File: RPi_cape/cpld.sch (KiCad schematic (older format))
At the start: 67 parts, among them P15 Conn_02x05_Odd_Even, Q10 MMBT3904, Q9 MMBT3904, U29 LP5907MFX-3.3, U30 LP5907MFX-1.8, U31 DNP (5M40ZE64), U32 MIC1557, U33 5M80ZT100 / 5M240ZT100

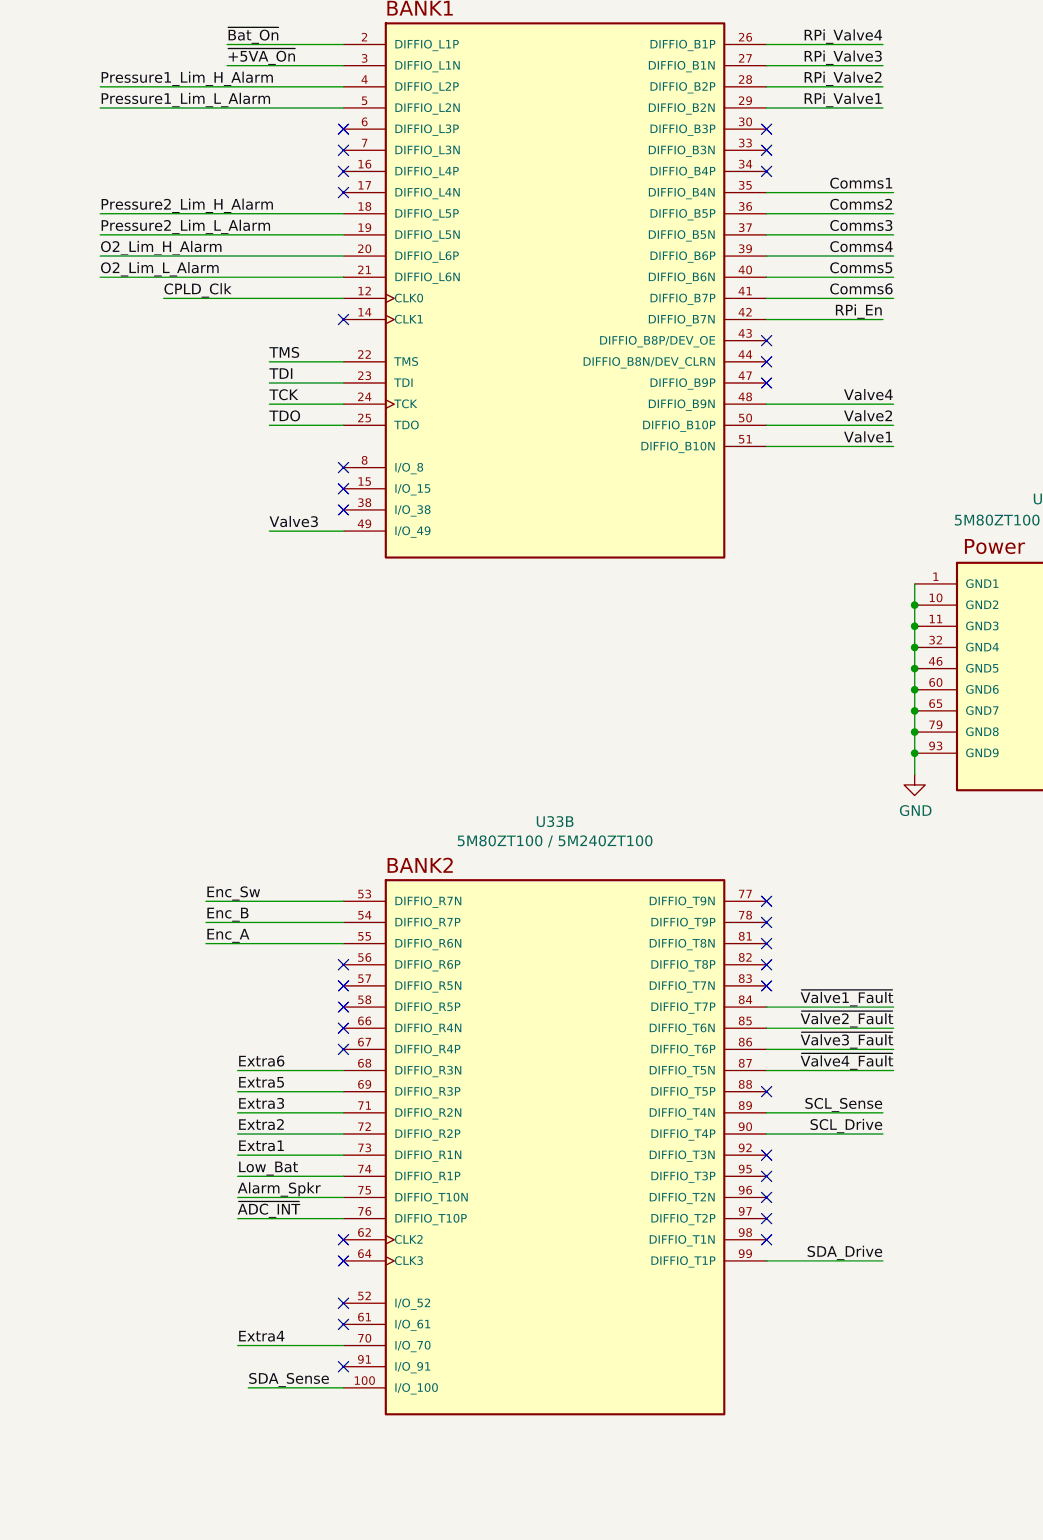
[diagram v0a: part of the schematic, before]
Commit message: Analog upgrades and extra encoder connectors
Renamed a few files
Removed "costing BOM" as difficult to keep up to date, easy to regenerate
Toughened under-voltage detect circuits by adding hysteresis to +5V detect for +BATT diode-OR (R236), filtering to power-down alarm detect input (C85)
Added connector options (J15, J21) for Grayhill C14-series rotary encoder with cable
Changed R190 from 3K to 2.4K to increase overhead on base current required for saturation, and consolidate BOM
Added 3 solderable testpoints for expanding CPLD pin options (TP44-46), adjusted some CPLD pin assignments to allow physical routing to pins
Fixed valve motion detector by changing comparator's hysteresis to AC-only, changing NPN's series resistor to 1K (allows low-enough DC level to count as logic low), and adding optional filtering cap C115 to offset divider
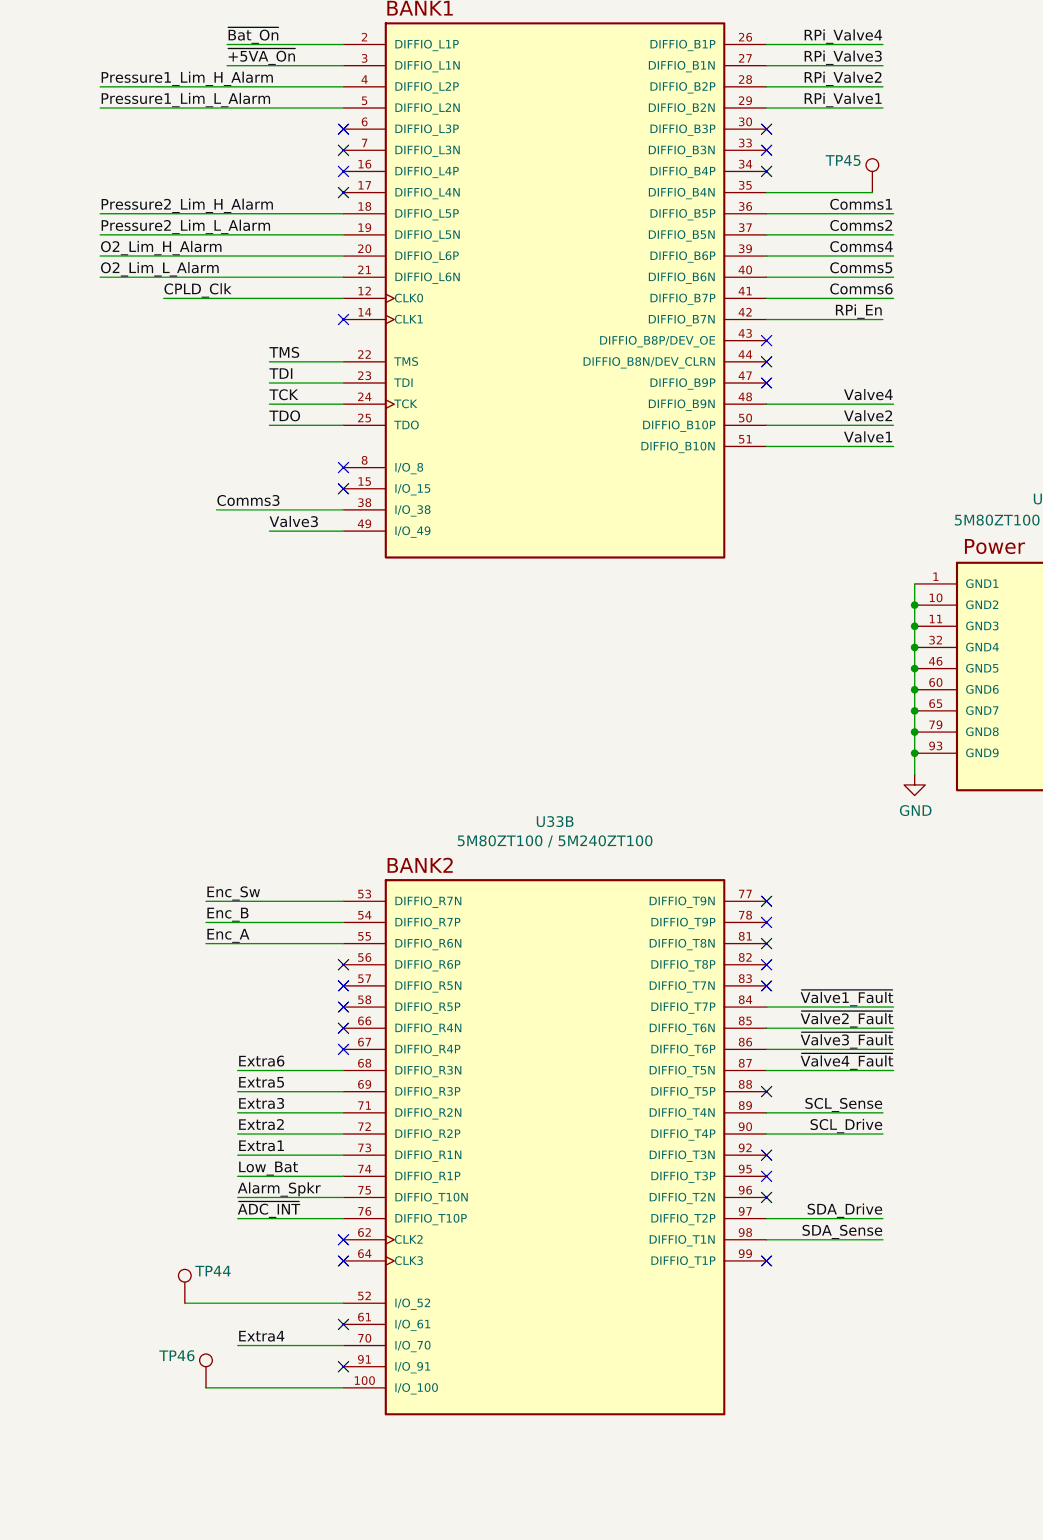
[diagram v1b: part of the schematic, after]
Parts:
- added TP44, TP45, TP46: TestPoint, TestPoint:TestPoint_Pad_1.0x1.0mm, symbol Connector:TestPoint
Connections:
- net Comms1: now also U33.36 (DIFFIO_B5P); no longer U33.35 (DIFFIO_B4N)
- net Comms2: now also U33.37 (DIFFIO_B5N); no longer U33.36 (DIFFIO_B5P)
- net Comms3: now also U33.38 (I/O_38); no longer U33.37 (DIFFIO_B5N)
- net SDA: now also U33.98 (DIFFIO_T1N); no longer U33.100 (I/O_100)
- net SDA_Drive: now also U33.97 (DIFFIO_T2P); no longer U33.99 (DIFFIO_T1P)
- net at U33.52 (I/O_52): now also TP44.1
- new net: TP45.1, U33.35 (DIFFIO_B4N)
- new net: TP46.1, U33.100 (I/O_100)
- no-connect marks 52 -> 49
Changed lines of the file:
@@
 encoding utf-8
 Sheet 15 15
-Title "CPLD"
+Title "Raspberry Pi Hat for JamVent Adaptation"
 Date ""
-Rev "1.7"
+Rev "1.8"
 Comp "US JamVent Team"
 Comment1 "Don Straney"
@@
 CPLD can be powered from backup battery when\nmain 5V power is out
 Wire Wire Line
-	12300 2300 12900 2300
-Text Label 12900 2300 2    50   ~ 0
-Comms1
-Wire Wire Line
 	12300 2400 12900 2400
 Text Label 12900 2400 2    50   ~ 0
-Comms2
+Comms1
 Wire Wire Line
 	12300 2500 12900 2500
 Text Label 12900 2500 2    50   ~ 0
+Comms2
+Wire Wire Line
+	10300 3800 9700 3800
+Text Label 9700 3800 0    50   ~ 0
 Comms3
 Wire Wire Line
@@
 Pressure1_Lim_H_Alarm
 Wire Wire Line
-	10300 7950 9850 7950
-Text Label 12850 7350 2    50   ~ 0
+	12300 7250 12850 7250
+Text Label 12850 7150 2    50   ~ 0
 SDA_Drive
-Text Label 9850 7950 0    50   ~ 0
+Text Label 12850 7250 2    50   ~ 0
 SDA_Sense
 Wire Wire Line
-	12850 7350 12300 7350
+	12850 7150 12300 7150
 Wire Wire Line
 	5450 8000 4750 8000
@@
 NoConn ~ 10300 7850
 NoConn ~ 10300 7650
-NoConn ~ 10300 7550
 NoConn ~ 10300 7350
 NoConn ~ 10300 7250
@@
 NoConn ~ 10300 3600
 NoConn ~ 10300 3700
-NoConn ~ 10300 3800
 NoConn ~ 12300 3000
 NoConn ~ 12300 3100
@@
 NoConn ~ 12300 6950
 NoConn ~ 12300 7050
-NoConn ~ 12300 7150
-NoConn ~ 12300 7250
 $Comp
 L Device:R R?
@@
 Wire Wire Line
 	9750 1700 10300 1700
+$Comp
+L Connector:TestPoint TP44
+U 1 1 5F052F66
+P 9550 7550
+F 0 "TP44" H 9600 7700 50  0000 L CNN
+F 1 "TestPoint" H 9608 7577 50  0001 L CNN
+F 2 "TestPoint:TestPoint_Pad_1.0x1.0mm" H 9750 7550 50  0001 C CNN
+F 3 "~" H 9750 7550 50  0001 C CNN
+	1    9550 7550
+	1    0    0    -1
+$EndComp
+Wire Wire Line
+	9550 7550 10300 7550
+$Comp
+L Connector:TestPoint TP46
+U 1 1 5F07D857
+P 9650 7950
+F 0 "TP46" H 9700 8100 50  0000 L CNN
+F 1 "TestPoint" H 9708 7977 50  0001 L CNN
+F 2 "TestPoint:TestPoint_Pad_1.0x1.0mm" H 9850 7950 50  0001 C CNN
+F 3 "~" H 9850 7950 50  0001 C CNN
+	1    9650 7950
+	-1   0    0    -1
+$EndComp
+Wire Wire Line
+	10300 7950 9650 7950
+$Comp
+L Connector:TestPoint TP45
+U 1 1 5F0937C5
+P 12800 2300
+F 0 "TP45" H 12850 2450 50  0000 L CNN
+F 1 "TestPoint" H 12858 2327 50  0001 L CNN
+F 2 "TestPoint:TestPoint_Pad_1.0x1.0mm" H 13000 2300 50  0001 C CNN
+F 3 "~" H 13000 2300 50  0001 C CNN
+	1    12800 2300
+	-1   0    0    -1
+$EndComp
+Wire Wire Line
+	12800 2300 12300 2300
+NoConn ~ 12300 7350
 $EndSCHEMATC

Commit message: Admin (naming, license), improvements based on testing
Updated name on schematic, PCB silkscreen
Added 3 mounting holes on inside area of board for better mechanical robustness
Removed extra unused pressure sensor barb packages from library
Fixed Phoenix spring connector footprints, and added 3D models from Phoenix website
Added 3D models to TE encoder connector footprints, QFP-100 for CPLD, and 5019 testpoint
Changed DIAG_EN pin connection from valve drivers from +24V (too high) to +3.3V
Added CERN licensing terms
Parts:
- TP21, TP22, TP23, TP24, TP25, TP26, TP27, TP28, TP42, TP43: footprint TestPoint:TestPoint_Keystone_5019_Minature -> Ventilator:TestPoint_Keystone_5019_Minature
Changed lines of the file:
@@
 encoding utf-8
 Sheet 15 15
-Title "Raspberry Pi Hat for JamVent Adaptation"
+Title "GlobalVent Stand-Alone Controller"
 Date ""
-Rev "1.9"
-Comp "US JamVent Team"
-Comment1 "Don Straney"
-Comment2 ""
+Rev "1.10"
+Comp "US GlobalVent Team"
+Comment1 "Licensed under CERN-OHL-S v2"
+Comment2 "Don Straney"
 Comment3 ""
 Comment4 ""
@@
 F 0 "TP27" H 2900 8750 50  0000 R CNN
 F 1 "TestPoint_Flag" H 2856 8653 50  0001 R CNN
-F 2 "TestPoint:TestPoint_Keystone_5019_Minature" H 3100 8650 50  0001 C CNN
+F 2 "Ventilator:TestPoint_Keystone_5019_Minature" H 3100 8650 50  0001 C CNN
 F 3 "~" H 3100 8650 50  0001 C CNN
 F 4 "Keystone" H 2900 8650 50  0001 C CNN "Manufacturer"
@@
 F 0 "TP28" H 2900 9800 50  0000 R CNN
 F 1 "TestPoint_Flag" H 2856 9703 50  0001 R CNN
-F 2 "TestPoint:TestPoint_Keystone_5019_Minature" H 3100 9700 50  0001 C CNN
+F 2 "Ventilator:TestPoint_Keystone_5019_Minature" H 3100 9700 50  0001 C CNN
 F 3 "~" H 3100 9700 50  0001 C CNN
 F 4 "Keystone" H 2900 9700 50  0001 C CNN "Manufacturer"
@@
 F 0 "TP22" H 2850 2950 50  0000 R CNN
 F 1 "TestPoint_Flag" H 2806 2853 50  0001 R CNN
-F 2 "TestPoint:TestPoint_Keystone_5019_Minature" H 3050 2850 50  0001 C CNN
+F 2 "Ventilator:TestPoint_Keystone_5019_Minature" H 3050 2850 50  0001 C CNN
 F 3 "~" H 3050 2850 50  0001 C CNN
 F 4 "Keystone" H 2850 2850 50  0001 C CNN "Manufacturer"
@@
 F 0 "TP23" H 2850 3150 50  0000 R CNN
 F 1 "TestPoint_Flag" H 2806 3053 50  0001 R CNN
-F 2 "TestPoint:TestPoint_Keystone_5019_Minature" H 3050 3050 50  0001 C CNN
+F 2 "Ventilator:TestPoint_Keystone_5019_Minature" H 3050 3050 50  0001 C CNN
 F 3 "~" H 3050 3050 50  0001 C CNN
 F 4 "Keystone" H 2850 3050 50  0001 C CNN "Manufacturer"
@@
 F 0 "TP24" H 2850 3350 50  0000 R CNN
 F 1 "TestPoint_Flag" H 2806 3253 50  0001 R CNN
-F 2 "TestPoint:TestPoint_Keystone_5019_Minature" H 3050 3250 50  0001 C CNN
+F 2 "Ventilator:TestPoint_Keystone_5019_Minature" H 3050 3250 50  0001 C CNN
 F 3 "~" H 3050 3250 50  0001 C CNN
 F 4 "Keystone" H 2850 3250 50  0001 C CNN "Manufacturer"
@@
 F 0 "TP25" H 2850 3550 50  0000 R CNN
 F 1 "TestPoint_Flag" H 2806 3453 50  0001 R CNN
-F 2 "TestPoint:TestPoint_Keystone_5019_Minature" H 3050 3450 50  0001 C CNN
+F 2 "Ventilator:TestPoint_Keystone_5019_Minature" H 3050 3450 50  0001 C CNN
 F 3 "~" H 3050 3450 50  0001 C CNN
 F 4 "Keystone" H 2850 3450 50  0001 C CNN "Manufacturer"
@@
 F 0 "TP26" H 2850 3750 50  0000 R CNN
 F 1 "TestPoint_Flag" H 2806 3653 50  0001 R CNN
-F 2 "TestPoint:TestPoint_Keystone_5019_Minature" H 3050 3650 50  0001 C CNN
+F 2 "Ventilator:TestPoint_Keystone_5019_Minature" H 3050 3650 50  0001 C CNN
 F 3 "~" H 3050 3650 50  0001 C CNN
 F 4 "Keystone" H 2850 3650 50  0001 C CNN "Manufacturer"
@@
 F 0 "TP21" H 2850 2750 50  0000 R CNN
 F 1 "TestPoint_Flag" H 2806 2653 50  0001 R CNN
-F 2 "TestPoint:TestPoint_Keystone_5019_Minature" H 3050 2650 50  0001 C CNN
+F 2 "Ventilator:TestPoint_Keystone_5019_Minature" H 3050 2650 50  0001 C CNN
 F 3 "~" H 3050 2650 50  0001 C CNN
 F 4 "Keystone" H 2850 2650 50  0001 C CNN "Manufacturer"
@@
 F 0 "TP42" H 1050 8500 50  0000 R CNN
 F 1 "TestPoint_Flag" H 756 8353 50  0001 R CNN
-F 2 "TestPoint:TestPoint_Keystone_5019_Minature" H 1000 8350 50  0001 C CNN
+F 2 "Ventilator:TestPoint_Keystone_5019_Minature" H 1000 8350 50  0001 C CNN
 F 3 "~" H 1000 8350 50  0001 C CNN
 F 4 "Keystone" H 800 8350 50  0001 C CNN "Manufacturer"
@@
 F 0 "TP43" H 1050 8800 50  0000 R CNN
 F 1 "TestPoint_Flag" H 756 8653 50  0001 R CNN
-F 2 "TestPoint:TestPoint_Keystone_5019_Minature" H 1000 8650 50  0001 C CNN
+F 2 "Ventilator:TestPoint_Keystone_5019_Minature" H 1000 8650 50  0001 C CNN
 F 3 "~" H 1000 8650 50  0001 C CNN
 F 4 "Keystone" H 800 8650 50  0001 C CNN "Manufacturer"

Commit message: Design update based on changed software/firmware/pneumatics reqs
Swapped Max V CPLD for Max 10 FPGA
Removed +1.8V regulator and monitoring (in power-down alarm) because Max 10 FPGA has internal regulator
Changed FPGA's valve-enable pull-downs from 1K to 10K because Max 10 floats the outputs during power-up/programming (instead of Max V's internal pull-ups)
Changed low-pressure sensor from BMP388 to MS5607 for more manufacturable footprint / high availability, and moved all digital pressure sensors to daughterboard for repairability
Changed single op-amps in analog pressure sensor inputs / valve motion detect circuits to TLV6001 for better bias current, correct footprint
Removed excessive DNP components in analog pressure sensor inputs to ease routing with new op-amps
Added double-inverted hysteresis circuit to valve motion detect that won't drive U38's '+' input above the rail and cause latchup
Added optional pull-down resistors to valve-motiion-detect op-amps to allow output voltages to swing to zero
Added optional filter caps to ADC sensor inputs
Added pull-down to O2 sensor input for testing with sensor unplugged
Increased ADC input resistors (in analog sensor inputs) from 1K to 3.3K to avoid "lifting" +3.3V rail voltage in case of fault
Increased hole sizes to 3.7 mm for fitting #6 screws, to match some threaded vibration-damping bumpers from Joost
Fixed F.Fab-layer component reference text in custom footprints
Updated manufacturing files
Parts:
- removed D46: Orange, Ventilator:LED_0805_2012Metric, symbol Device:LED
- removed Q10, Q9: MMBT3904, Ventilator:SOT-23, symbol Transistor_BJT:MMBT3904
- removed TP28: TestPoint_Flag, Ventilator:TestPoint_Keystone_5019_Minature, symbol Connector:TestPoint_Flag
- removed U30: LP5907MFX-1.8, Ventilator:SOT-23-5, symbol Regulator_Linear:LP5907MFX-1.8
- removed U31: DNP (5M40ZE64), Ventilator:QFP40P900X900X120-65N, symbol Ventilator:5M40ZE64C5N
- removed U33: 5M80ZT100 / 5M240ZT100, Ventilator:QFP50P1600X1600X120-100N, symbol Ventilator:5M80ZT100C5N
- added C116, C117, C118, C119, C120, C121, C123, C124, C125, C126, C127, C128, C129, C130, C131, C132, C133: 100nF 50V X7R, Capacitor_SMD:C_0603_1608Metric, symbol Device:C
- added C122, C136, C137: 10pF 50V NP0, Capacitor_SMD:C_0603_1608Metric, symbol Device:C
- added C134, C135: 1uF 16V X7R, Capacitor_SMD:C_0805_2012Metric, symbol Device:C
- added D14, D2: BAT54C, Package_TO_SOT_SMD:SOT-23, symbol Device:D_Schottky_x2_KCom_AAK
- added FB1: TBD, Inductor_SMD:L_0805_2012Metric, symbol Device:Ferrite_Bead
- added R131, R132, R237, R238, R239: 10K, Resistor_SMD:R_1206_3216Metric, symbol Device:R
- added R221: 0, Resistor_SMD:R_1206_3216Metric, symbol Device:R
- added U30: 10M08SAE144C8G, Ventilator:LQFP50P2200X2200X160-145N, symbol Ventilator:10M08SAE144C8G
- C71, C73: value 1uF 16V X7R -> 100nF 50V X7R; footprint Capacitor_SMD:C_0805_2012Metric -> Capacitor_SMD:C_0603_1608Metric; Manufacturer Kemet -> AVX; Part Number C0805C105K4RACTU -> 06035C104JAT2A
- C74, P15, R186: DNI (none) -> DNI
- C75: value DNP -> 100nF 50V X7R; footprint Capacitor_SMD:C_1210_3225Metric -> Capacitor_SMD:C_0603_1608Metric; Manufacturer (none) -> AVX; Part Number (none) -> 06035C104JAT2A
- C86: value 1uF 16V X7R -> 10pF 50V NP0; footprint Capacitor_SMD:C_0805_2012Metric -> Capacitor_SMD:C_0603_1608Metric; Manufacturer Kemet -> (none); Part Number C0805C105K4RACTU -> (none)
- R152: value 10K -> 1K; Part Number RK73H2BTTD1002F -> RK73H2BTTD1001F
- R153: value 10K -> 0; Manufacturer KOA Speer -> Panasonic; Part Number RK73H2BTTD1002F -> ERJ-8GEY0R00V
- R154: value 10K -> DNP; DNI (none) -> DNI; Manufacturer KOA Speer -> (none); Part Number RK73H2BTTD1002F -> (none)
- R159: value 100 -> 10K; Part Number RK73H2BTTD1000F -> RK73H2BTTD1002F
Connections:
- net SCL_Drive is gone; now on an unnamed net: R154.2
- net SDA_Drive is gone; now on net +3V3: R153.2
- net +3V3: now also C71.2, C73.2, C75.2, C87.2, C90.2, R159.1, C116.2, C117.2, C118.2, C120.2, C121.2, C123.2, C124.2, C126.2, C127.2, C129.2, C131.2, C133.2, C135.2, D14.3 (K), D2.3 (K), FB1.1, R131.1, R132.1, R221.2, R237.1, R238.1, R239.1, U30.1 (VCC_ONE1), U30.103 (VCCIO6_2), U30.108 (VCC_ONE7), U30.109 (VCC_ONE8), U30.115 (VCC_ONE9), U30.117 (VCCIO7), U30.128 (VCCIO8_1), U30.139 (VCCIO8_2), U30.144 (VCC_ONE10), U30.23 (VCCIO1B), U30.31 (VCCIO2), U30.36 (VCC_ONE2), U30.37 (VCC_ONE3), U30.40 (VCCIO3_1), U30.49 (VCCIO3_2), U30.5 (ADC_VREF), U30.51 (VCC_ONE4), U30.67 (VCCIO4), U30.72 (VCC_ONE5), U30.73 (VCC_ONE6), U30.82 (VCCIO5), U30.9 (VCCIO1A), U30.94 (VCCIO6_1)
- net Alarm_Spkr: now also U30.111 (IO,(DIFFIO_RX_T1N,DIFFOUT_T1N))
- net CPLD_Clk: now also U30.27 (IO,CLK0P,(DIFFIO_RX_L18P,DIFFOUT_L18P))
- net Comms1: now also U30.56 (IO,(DIFFIO_TX_RX_B12P,DIFFOUT_B12P))
- net Comms2: now also U30.57 (IO,(DIFFIO_TX_RX_B14N,DIFFOUT_B14N))
- net Comms3: now also U30.58 (IO,(DIFFIO_TX_RX_B14P,DIFFOUT_B14P))
- net Comms4: now also U30.59 (IO,(DIFFIO_TX_RX_B16N,DIFFOUT_B16N))
- net Comms5: now also U30.60 (IO,(DIFFIO_TX_RX_B16P,DIFFOUT_B16P))
- net Comms6: now also U30.61 (IO,VREFB4N0)
- net Enc_A: now also U30.87 (IO,(DIFFIO_RX_R10N,DIFFOUT_R10N))
- net Enc_B: now also U30.86 (IO,(DIFFIO_RX_R11N,DIFFOUT_R11N))
- net Enc_Sw: now also U30.79 (IO,(DIFFIO_RX_R7P,DIFFOUT_R7P))
- net Extra1: now also U30.100 (IO,(DIFFIO_RX_R28P,DIFFOUT_R28P))
- net Extra2: now also U30.99 (IO,(DIFFIO_RX_R27P,DIFFOUT_R27P))
- net Extra3: now also U30.98 (IO,DPCLK2,(DIFFIO_RX_R26N,DIFFOUT_R26N))
- net Extra4: now also U30.90 (IO,CLK3P,(DIFFIO_RX_R16P,DIFFOUT_R16P))
- net Extra5: now also U30.89 (IO,CLK2N,(DIFFIO_RX_R14N,DIFFOUT_R14N))
- net Extra6: now also U30.88 (IO,CLK2P,(DIFFIO_RX_R14P,DIFFOUT_R14P))
- net GND: now also C75.1, R154.1, C116.1, C117.1, C118.1, C119.1, C120.1, C121.1, C122.1, C123.1, C124.1, C125.1, C126.1, C127.1, C128.1, C129.1, C130.1, C131.1, C132.1, C133.1, C134.1, C135.1, C136.1, C137.1, U30.104 (GND7), U30.116 (GND8), U30.122 (IO,DEV_OE), U30.125 (GND9), U30.133 (GND10), U30.137 (GND11), U30.142 (GND12), U30.145 (EXP), U30.3 (ANAIN1), U30.4 (REFGND), U30.42 (GND1), U30.53 (GND2), U30.63 (GND3), U30.68 (GND4), U30.83 (GND5), U30.95 (GND6); no longer C75.2
- net Low_Bat: now also U30.102 (IO,(DIFFIO_RX_R28N,DIFFOUT_R28N))
- net O2_Lim_H_Alarm: now also U30.11 (IO,ADC1IN5,(DIFFIO_RX_L5N,DIFFOUT_L5N))
- net O2_Lim_L_Alarm: now also U30.12 (IO,ADC1IN6,(DIFFIO_RX_L5P,DIFFOUT_L5P))
- net Pressure1_Lim_H_Alarm: now also U30.6 (IO,ADC1IN1,(DIFFIO_RX_L1N,DIFFOUT_L1N))
- net Pressure1_Lim_L_Alarm: now also U30.7 (IO,ADC1IN2,(DIFFIO_RX_L1P,DIFFOUT_L1P))
- net Pressure2_Lim_H_Alarm: now also U30.8 (IO,ADC1IN3,(DIFFIO_RX_L3N,DIFFOUT_L3N))
- net Pressure2_Lim_L_Alarm: now also U30.10 (IO,ADC1IN4,(DIFFIO_RX_L3P,DIFFOUT_L3P))
- net RPi_En: now also U30.62 (IO4_1)
- net RPi_Valve1: now also U30.47 (IO,(DIFFIO_TX_RX_B7P,DIFFOUT_B7P))
- net RPi_Valve2: now also U30.46 (IO,(DIFFIO_TX_RX_B7N,DIFFOUT_B7N))
- net RPi_Valve3: now also U30.45 (IO,(DIFFIO_TX_RX_B5P,DIFFOUT_B5P))
- net RPi_Valve4: now also U30.44 (IO,(DIFFIO_TX_RX_B5N,DIFFOUT_B5N))
- net SCL: now also U30.131 (IO,(DIFFIO_RX_T20N,DIFFOUT_T20N))
- net SDA: now also U30.132 (IO,(DIFFIO_RX_T22P,DIFFOUT_T22P))
- net TCK: now also C136.2, D2.2 (A), U30.18 (IO,TCK,(DIFFIO_RX_L11P,DIFFOUT_L11P))
- net TDI: now also C86.2, D14.2 (A), R238.2, U30.19 (IO,TDI,(DIFFIO_RX_L12N,DIFFOUT_L12N))
- net TDO: now also C137.2, D14.1 (A), U30.20 (IO,TDO,(DIFFIO_RX_L12P,DIFFOUT_L12P))
- net TMS: now also C122.2, D2.1 (A), R239.2, U30.16 (IO,TMS,(DIFFIO_RX_L11N,DIFFOUT_L11N))
- net Valve1: now also U30.78 (IO5_1)
- net Valve2: now also U30.77 (IO,(DIFFIO_RX_R1N,DIFFOUT_R1N))
- net Valve3: now also U30.76 (IO,(DIFFIO_RX_R2N,DIFFOUT_R2N))
- net Valve4: now also U30.75 (IO,(DIFFIO_RX_R1P,DIFFOUT_R1P))
- net ~+5VA_On: now also U30.101 (IO,(DIFFIO_RX_R27N,DIFFOUT_R27N))
- net ~ADC_INT: now also U30.130 (IO,(DIFFIO_RX_T20P,DIFFOUT_T20P))
- net ~Bat_On: now also U30.106 (IO,(DIFFIO_RX_R33N,DIFFOUT_R33N))
- net ~Valve1_Fault: now also U30.119 (IO,(DIFFIO_RX_T10N,DIFFOUT_T10N))
- net ~Valve2_Fault: now also U30.120 (IO,(DIFFIO_RX_T16P,DIFFOUT_T16P))
- net ~Valve3_Fault: now also U30.123 (IO,VREFB8N0)
- net ~Valve4_Fault: now also U30.124 (IO,(DIFFIO_RX_T19P,DIFFOUT_T19P))
- net at TP45.1: now also U30.91 (IO,CLK3N,(DIFFIO_RX_R16N,DIFFOUT_R16N))
- net at TP46.1: now also U30.135 (IO8_1)
- net at TP44.1: now also U30.14 (IO,ADC1IN8,(DIFFIO_RX_L7P,DIFFOUT_L7P))
- net at C70.2, R185.1, R186.1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: no longer C71.2
- net at R153.1: now also U30.126 (IO,CONFIG_SEL)
- removed net +1V8: C73.2, C75.1, C86.2, C87.2, C90.2, R159.2
- new net: R221.1, U30.121 (IO,DEV_CLRN,(DIFFIO_RX_T16N,DIFFOUT_T16N))
- new net: R237.2, U30.129 (NCONFIG)
- new net: R159.2, U30.134 (IO,CRC_ERROR,(DIFFIO_RX_T22N,DIFFOUT_T22N))
- new net: R131.2, U30.138 (IO,CONF_DONE,(DIFFIO_RX_T24N,DIFFOUT_T24N))
- new net +3.3VA: C119.2, C125.2, C128.2, C130.2, C132.2, C134.2, FB1.2, U30.107 (VCCA3), U30.143 (VCCA4), U30.2 (VCCA6), U30.34 (VCCA2), U30.35 (VCCA1), U30.71 (VCCA5)
- new net ~FPGA_RST: R132.2, U30.136 (IO,NSTATUS,(DIFFIO_RX_T24P,DIFFOUT_T24P))
- no-connect marks 49 -> 48
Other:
- note added: "Global register reset\nwhen held low"
- note added: "High if CRC errors\nin config. mem."
- note added: "High when config.\nis done"
- note added: "Low during power-on\nreset and if errors\nduring config."
- note added: "Overshoot prevention\ncircuit recommended\nby Max 10 docs"
- note added: "Rising edge\ninitiates config."
- note added: "Selects config.\nimage 0 (low) or\n1 (high)"
- note removed: "40 mA from +1.8V"
- note removed: "Keep <10uF on +1.8V for LP5907 stability"
- note removed: "Populate either 5M40Z (left) or 5M80Z (right)"
- moved on the sheet: C70, C72, C74, C76, C79, C87, C88, C89, C90, C91, C92, C93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
